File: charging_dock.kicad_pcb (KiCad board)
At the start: 2 copper layers, 38 x 38 mm, 8 parts, among them J1 USB4105-GF-A, J2 Charging Pad+, J3 Charging Pad-, J4 Charging Pad+, J5 Charging Pad+

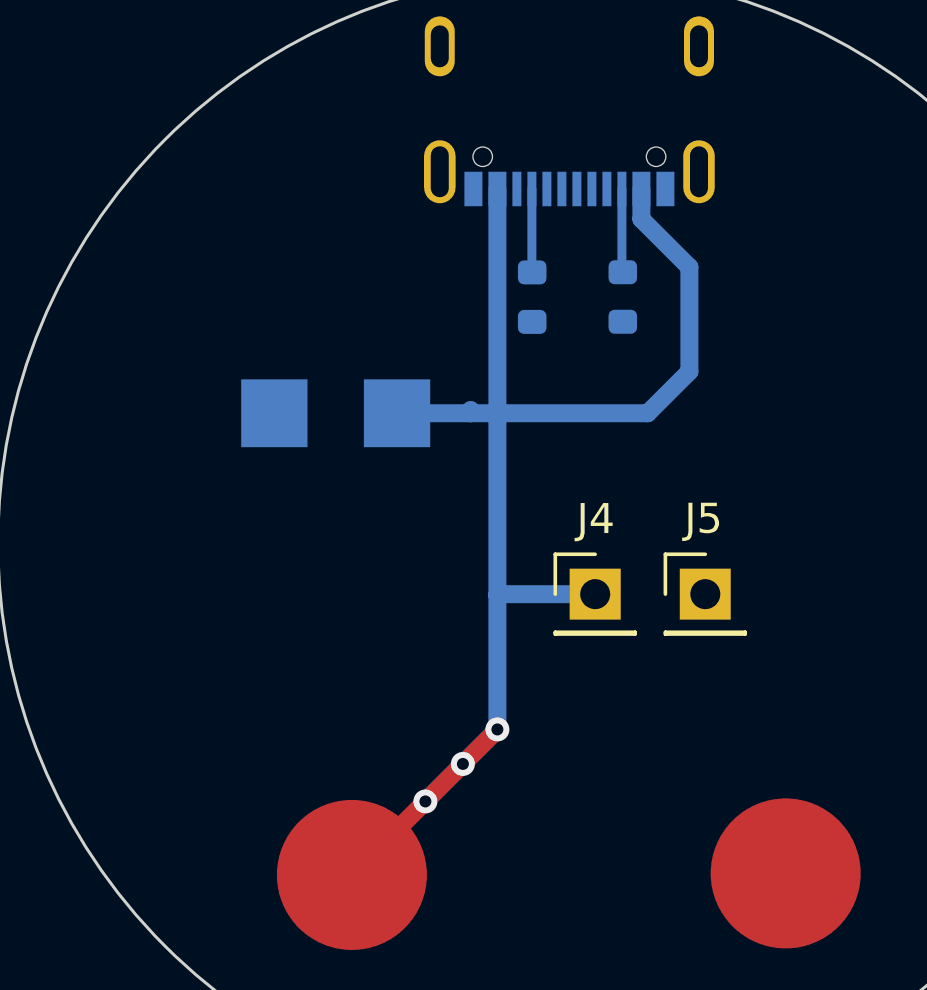
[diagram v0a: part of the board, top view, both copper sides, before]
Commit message: added hole for hr-sensor
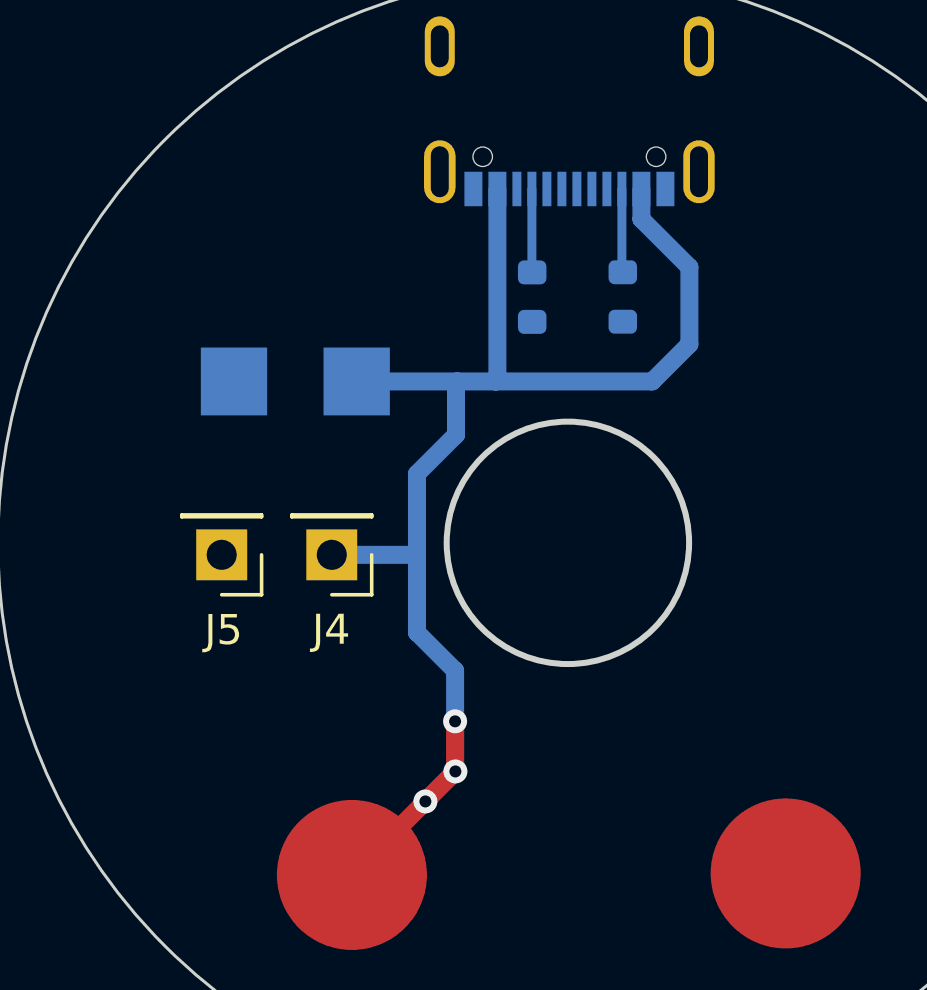
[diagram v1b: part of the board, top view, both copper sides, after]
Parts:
- moved J5 16.2 mm to (141.0, 94.0), turned to 180 degrees
- moved J4 8.88 mm to (144.6, 94.0), turned to 180 degrees
- moved CR1 1.71 mm to (143.4, 88.3)
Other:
- outline, holes or cut-outs redrawn
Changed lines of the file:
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@@
   )
   (footprint "Connector_PinHeader_2.54mm:PinHeader_1x01_P2.54mm_Vertical" (layer "F.Cu")
-    (at 157.09 95.35)
+    (at 140.97 94.04 180)
     (descr "Through hole straight pin header, 1x01, 2.54mm pitch, single row")
     (tags "Through hole pin header THT 1x01 2.54mm single row")
@@
     (fp_line (start 1.27 1.27) (end -1.27 1.27)
       (stroke (width 0.1) (type solid)) (layer "F.Fab"))
-    (pad "1" thru_hole rect (at 0 0) (size 1.7 1.7) (drill 1) (layers "*.Cu" "*.Mask")
+    (pad "1" thru_hole rect (at 0 0 180) (size 1.7 1.7) (drill 1) (layers "*.Cu" "*.Mask")
       (net 2 "GND") (pinfunction "Pin_1") (pintype "passive"))
   )
   (footprint "Connector_PinHeader_2.54mm:PinHeader_1x01_P2.54mm_Vertical" (layer "F.Cu")
-    (at 153.42 95.35)
+    (at 144.64 94.04 180)
     (descr "Through hole straight pin header, 1x01, 2.54mm pitch, single row")
     (tags "Through hole pin header THT 1x01 2.54mm single row")
@@
     (fp_line (start 1.27 1.27) (end -1.27 1.27)
       (stroke (width 0.1) (type solid)) (layer "F.Fab"))
-    (pad "1" thru_hole rect (at 0 0) (size 1.7 1.7) (drill 1) (layers "*.Cu" "*.Mask")
+    (pad "1" thru_hole rect (at 0 0 180) (size 1.7 1.7) (drill 1) (layers "*.Cu" "*.Mask")
       (net 1 "Net-(J2-Pin_1)") (pinfunction "Pin_1") (pintype "passive"))
   )
@@
   )
   (footprint "SMBJ5-0A-TR:SMB_STM" (layer "B.Cu")
-    (at 144.77 89.32 180)
+    (at 143.4245 88.26 180)
     (tags "SMBJ5.0A-TR ")
     (property "Sheetfile" "charging_dock.kicad_sch")
@@
       (polygon
         (pts
-          (xy 145.659 87.3896)
-          (xy 143.881 87.3896)
-          (xy 143.881 91.2504)
-          (xy 145.659 91.2504)
+          (xy 144.3135 86.3296)
+          (xy 142.5355 86.3296)
+          (xy 142.5355 90.1904)
+          (xy 144.3135 90.1904)
         )
       )
@@
     )
   )
+  (gr_circle (center 152.51 93.64) (end 156.55 93.64)
+    (stroke (width 0.2) (type default)) (fill none) (layer "Edge.Cuts"))
   (gr_circle (center 152.51 93.64) (end 171.51 93.64)
     (stroke (width 0.1) (type default)) (fill none) (layer "Edge.Cuts"))
+  (segment (start 148.75 101.25) (end 148.75 99.59) (width 0.6) (layer "F.Cu") (net 1))
   (segment (start 147.76 102.26) (end 145.31 104.71) (width 0.6) (layer "F.Cu") (net 1))
-  (segment (start 149.01 101.01) (end 147.76 102.26) (width 0.6) (layer "F.Cu") (net 1))
-  (segment (start 150.16 99.86) (end 149.01 101.01) (width 0.6) (layer "F.Cu") (net 1))
-  (via (at 149.01 101.01) (size 0.8) (drill 0.4) (layers "F.Cu" "B.Cu") (net 1))
-  (via (at 150.16 99.86) (size 0.8) (drill 0.4) (layers "F.Cu" "B.Cu") (net 1))
+  (segment (start 148.76 101.26) (end 148.75 101.25) (width 0.6) (layer "F.Cu") (net 1))
+  (segment (start 148.76 101.26) (end 147.76 102.26) (width 0.6) (layer "F.Cu") (net 1))
+  (via (at 148.76 101.26) (size 0.8) (drill 0.4) (layers "F.Cu" "B.Cu") (net 1))
+  (via (at 148.75 99.59) (size 0.8) (drill 0.4) (layers "F.Cu" "B.Cu") (net 1))
   (via (at 147.76 102.26) (size 0.8) (drill 0.4) (layers "F.Cu" "B.Cu") (net 1))
-  (segment (start 150.18 89.32) (end 149.27 89.32) (width 0.6) (layer "B.Cu") (net 1))
-  (segment (start 150.16 99.86) (end 149.01 101.01) (width 0.6) (layer "B.Cu") (net 1))
-  (segment (start 150.16 99.86) (end 150.16 95.38) (width 0.6) (layer "B.Cu") (net 1))
-  (segment (start 155.17 89.32) (end 150.18 89.32) (width 0.6) (layer "B.Cu") (net 1))
-  (segment (start 150.16 89.3) (end 150.18 89.32) (width 0.6) (layer "B.Cu") (net 1))
-  (segment (start 150.19 95.35) (end 153.42 95.35) (width 0.6) (layer "B.Cu") (net 1))
-  (segment (start 150.16 81.845) (end 150.16 89.3) (width 0.6) (layer "B.Cu") (net 1))
-  (segment (start 156.56 84.45) (end 156.56 87.93) (width 0.6) (layer "B.Cu") (net 1))
-  (segment (start 149.27 89.32) (end 146.8147 89.32) (width 0.6) (layer "B.Cu") (net 1))
-  (segment (start 156.56 87.93) (end 155.17 89.32) (width 0.6) (layer "B.Cu") (net 1))
-  (segment (start 149.27 89.21) (end 149.27 89.32) (width 0.6) (layer "B.Cu") (net 1))
+  (segment (start 148.78 88.3) (end 148.78 90.04) (width 0.6) (layer "B.Cu") (net 1))
+  (segment (start 150.16 88.2) (end 150.1 88.26) (width 0.6) (layer "B.Cu") (net 1))
+  (segment (start 148.82 88.26) (end 148.78 88.3) (width 0.6) (layer "B.Cu") (net 1))
+  (segment (start 154.96 82.85) (end 156.56 84.45) (width 0.6) (layer "B.Cu") (net 1))
+  (segment (start 156.56 84.45) (end 156.56 87.02) (width 0.6) (layer "B.Cu") (net 1))
+  (segment (start 148.78 90.04) (end 147.48 91.34) (width 0.6) (layer "B.Cu") (net 1))
+  (segment (start 148.75 97.9) (end 148.75 99.59) (width 0.6) (layer "B.Cu") (net 1))
+  (segment (start 148.82 88.26) (end 145.4692 88.26) (width 0.6) (layer "B.Cu") (net 1))
+  (segment (start 147.48 91.34) (end 147.48 93.9) (width 0.6) (layer "B.Cu") (net 1))
+  (segment (start 147.48 96.63) (end 148.75 97.9) (width 0.6) (layer "B.Cu") (net 1))
+  (segment (start 148.76 101.26) (end 147.76 102.26) (width 0.6) (layer "B.Cu") (net 1))
+  (segment (start 150.1 88.26) (end 148.82 88.26) (width 0.6) (layer "B.Cu") (net 1))
+  (segment (start 148.75 101.25) (end 148.75 99.59) (width 0.6) (layer "B.Cu") (net 1))
+  (segment (start 148.76 101.26) (end 148.75 101.25) (width 0.6) (layer "B.Cu") (net 1))
+  (segment (start 155.32 88.26) (end 150.1 88.26) (width 0.6) (layer "B.Cu") (net 1))
+  (segment (start 147.48 93.9) (end 147.48 96.63) (width 0.6) (layer "B.Cu") (net 1))
+  (segment (start 156.56 87.02) (end 155.32 88.26) (width 0.6) (layer "B.Cu") (net 1))
+  (segment (start 147.34 94.04) (end 144.64 94.04) (width 0.6) (layer "B.Cu") (net 1))
+  (segment (start 150.16 81.845) (end 150.16 88.2) (width 0.6) (layer "B.Cu") (net 1))
   (segment (start 154.96 81.845) (end 154.96 82.85) (width 0.6) (layer "B.Cu") (net 1))
-  (segment (start 150.16 95.38) (end 150.16 89.3) (width 0.6) (layer "B.Cu") (net 1))
-  (segment (start 150.16 95.38) (end 150.19 95.35) (width 0.6) (layer "B.Cu") (net 1))
-  (segment (start 154.96 82.85) (end 156.56 84.45) (width 0.6) (layer "B.Cu") (net 1))
-  (segment (start 149.01 101.01) (end 147.76 102.26) (width 0.6) (layer "B.Cu") (net 1))
+  (segment (start 147.48 93.9) (end 147.34 94.04) (width 0.6) (layer "B.Cu") (net 1))
   (segment (start 151.31 84.615) (end 151.32 84.625) (width 0.25) (layer "B.Cu") (net 8))
   (segment (start 151.31 81.845) (end 151.31 84.615) (width 0.3) (layer "B.Cu") (net 8))
